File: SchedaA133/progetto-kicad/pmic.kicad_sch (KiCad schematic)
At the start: 65 parts, among them SW201 PWRON, U201 AXP717, U202 AP2112K-3.3, U203 TPS563201

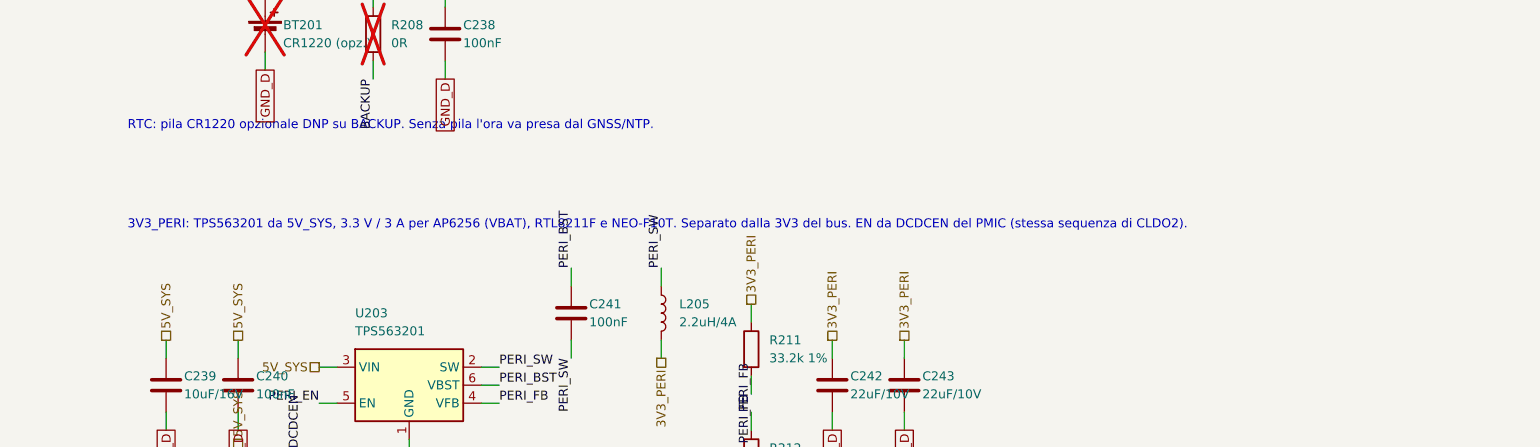
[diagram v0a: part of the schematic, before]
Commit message: SchedaA133: NEO-F10T sostituito dal NEO-M9N-00B
- Simbolo RF_GPS:NEO-M9N, pin verificati sul data sheet UBX-19014285 R08 (tabella 9)
- Collegamenti invariati sui pin comuni; V_USB (pin 7) ora a GND, D_SEL, USB, LNA_EN, SDA/SCL liberi
- README, bom-a133.csv (U10) e documenti aggiornati, eMMC resta 256 GB
- ERC 0, schema-a133.pdf riesportato

Co-Authored-By: Claude Opus 5.5 (1M context) <noreply@anthropic.com>
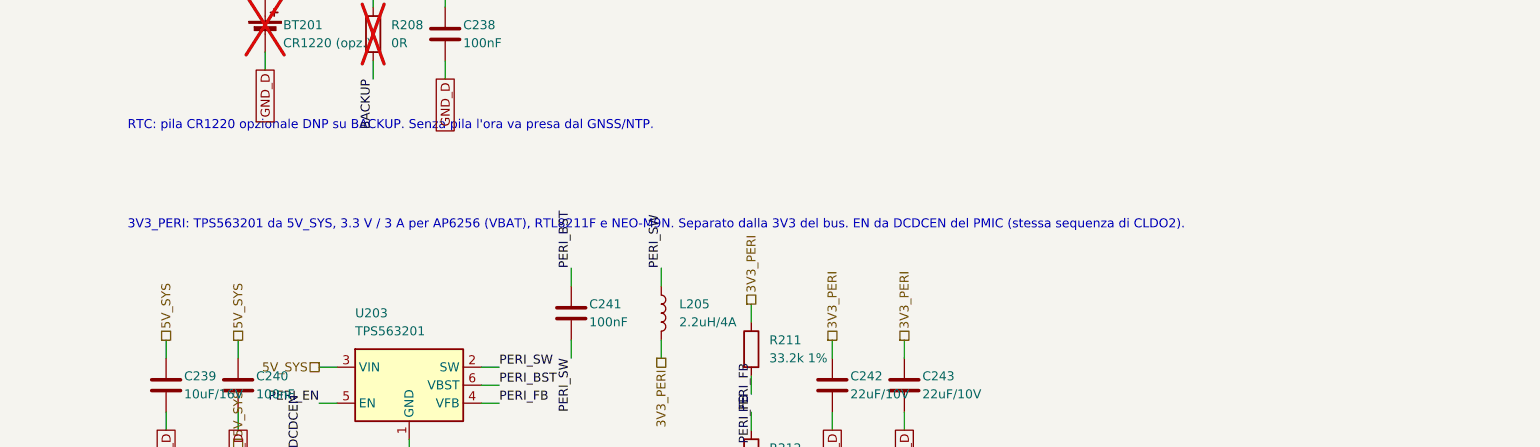
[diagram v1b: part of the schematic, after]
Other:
- note added: "3V3_PERI: TPS563201 da 5V_SYS, 3.3 V / 3 A per AP6256 (VBAT), RTL8211F e NEO-M9N. Separato dalla 3V3 del bus. EN da DCDCEN del PMIC (stessa sequenza di CLDO2)."
- note removed: "3V3_PERI: TPS563201 da 5V_SYS, 3.3 V / 3 A per AP6256 (VBAT), RTL8211F e NEO-F10T. Separato dalla 3V3 del bus. EN da DCDCEN del PMIC (stessa sequenza di CLDO2)."
